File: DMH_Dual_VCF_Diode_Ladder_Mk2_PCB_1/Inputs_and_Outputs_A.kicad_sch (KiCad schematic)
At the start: 8 parts, among them J1 TS_Jack_6.35mm_Sw, J2 TS_Jack_6.35mm_Sw, J200 IDC_02x05, J3 TS_Jack_6.35mm_Sw, J4 TS_Jack_6.35mm_Sw, J5 TS_Jack_6.35mm_Sw, J6 TS_Jack_6.35mm_Sw, J7 TS_Jack_6.35mm_Sw

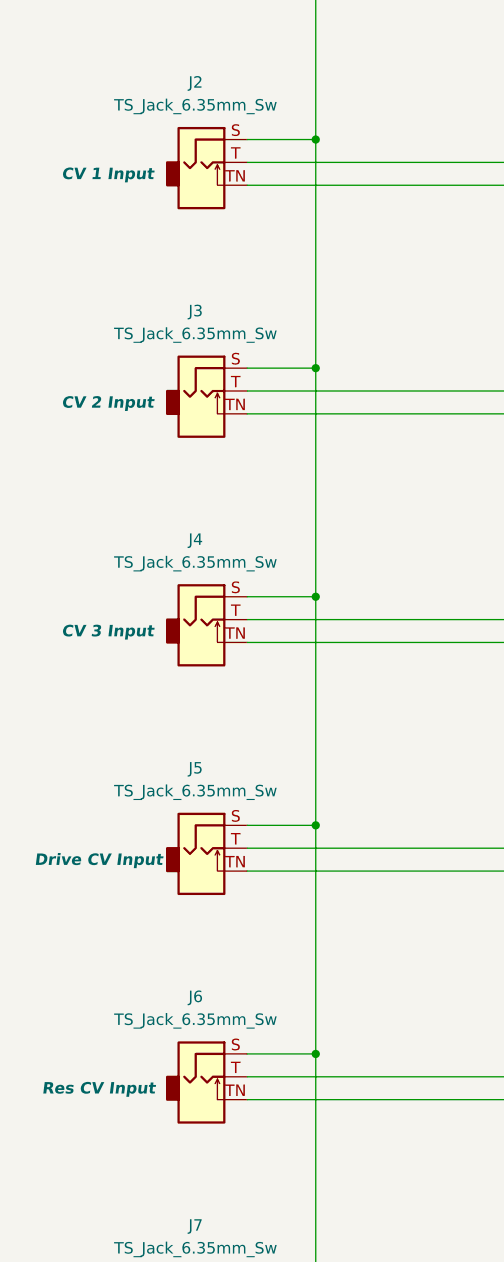
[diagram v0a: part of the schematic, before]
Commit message: Routed circuit B
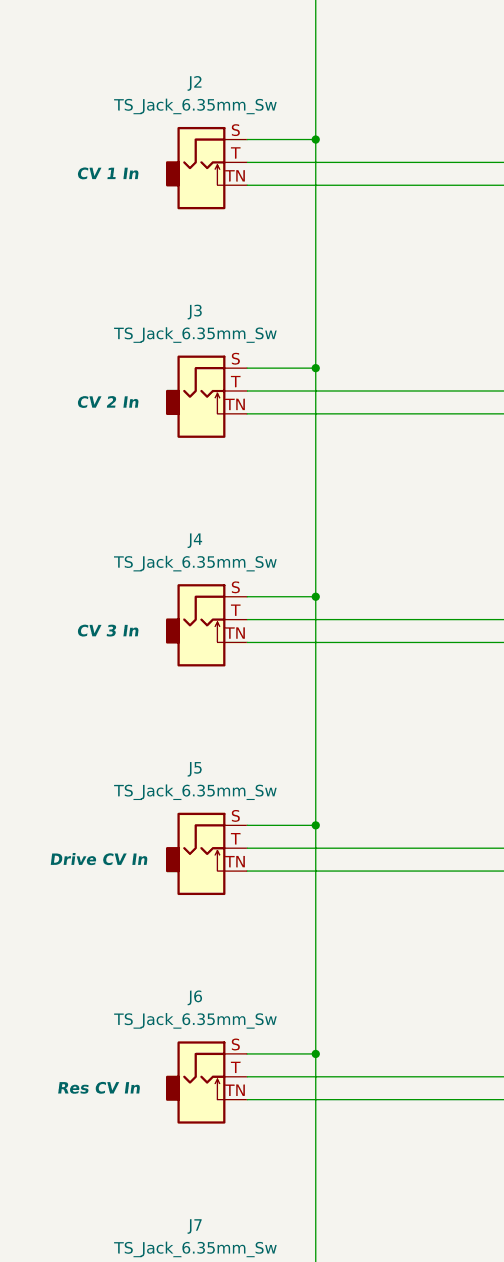
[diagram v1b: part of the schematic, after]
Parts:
- J2: Function CV 1 Input -> CV 1 In
- J3: Function CV 2 Input -> CV 2 In
- J4: Function CV 3 Input -> CV 3 In
- J5: Function Drive CV Input -> Drive CV In
- J6: Function Res CV Input -> Res CV In
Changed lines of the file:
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@@
 			)
 		)
-		(property "Function" "Drive CV Input"
+		(property "Function" "Drive CV In"
 			(at 39.37 140.97 0)
 			(effects
@@
 			)
 		)
-		(property "Function" "CV 3 Input"
+		(property "Function" "CV 3 In"
 			(at 40.386 115.57 0)
 			(effects
@@
 			)
 		)
-		(property "Function" "CV 1 Input"
+		(property "Function" "CV 1 In"
 			(at 40.386 64.77 0)
 			(effects
@@
 			)
 		)
-		(property "Function" "Res CV Input"
+		(property "Function" "Res CV In"
 			(at 39.37 166.37 0)
 			(effects
@@
 			)
 		)
-		(property "Function" "CV 2 Input"
+		(property "Function" "CV 2 In"
 			(at 40.386 90.17 0)
 			(effects
